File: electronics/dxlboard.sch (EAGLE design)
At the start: 49 parts

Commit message: Boards
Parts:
- R1, R12, R13, R14, R15, R18, R19, R2, R20, R21, R3, R4: value (none) -> 3K
- R7S1, R7S2, R8S, R8S1, R8S2, R8S3: value 20 -> 22
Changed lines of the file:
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@@
 <part name="C2" library="SparkFun-Passives" deviceset="CAP_POL" device="PTH2"/>
 <part name="GND15" library="supply1" deviceset="GND" device=""/>
-<part name="R1" library="rhoban" deviceset="RESISTANCE" device="-R0805"/>
-<part name="R2" library="rhoban" deviceset="RESISTANCE" device="-R0805"/>
-<part name="R3" library="rhoban" deviceset="RESISTANCE" device="-R0805"/>
+<part name="R1" library="rhoban" deviceset="RESISTANCE" device="-R0805" value="3K"/>
+<part name="R2" library="rhoban" deviceset="RESISTANCE" device="-R0805" value="3K"/>
+<part name="R3" library="rhoban" deviceset="RESISTANCE" device="-R0805" value="3K"/>
 <part name="GND23" library="supply1" deviceset="GND" device=""/>
 <part name="P+16" library="supply1" deviceset="VCC" device=""/>
 <part name="CA" library="rhoban" deviceset="C_EU" device="-100NF"/>
-<part name="R8S" library="rhoban" deviceset="RESISTANCE" device="-R0805" value="20"/>
+<part name="R8S" library="rhoban" deviceset="RESISTANCE" device="-R0805" value="22"/>
 <part name="USB" library="rhoban" deviceset="CONNEC_1X04" device=""/>
 <part name="GND16" library="supply1" deviceset="GND" device=""/>
@@
 <part name="R9" library="rhoban" deviceset="RESISTANCE" device="-R0805"/>
 <part name="GND18" library="supply1" deviceset="GND" device=""/>
-<part name="R4" library="rhoban" deviceset="RESISTANCE" device="-R0805"/>
+<part name="R4" library="rhoban" deviceset="RESISTANCE" device="-R0805" value="3K"/>
 <part name="P+1" library="supply1" deviceset="VCC" device=""/>
 <part name="GPIO1" library="rhoban" deviceset="CONNEC_1X09" device=""/>
@@
 <part name="GND5" library="supply1" deviceset="GND" device=""/>
 <part name="P+4" library="supply1" deviceset="VCC" device=""/>
-<part name="R12" library="rhoban" deviceset="RESISTANCE" device="-R0805"/>
-<part name="R13" library="rhoban" deviceset="RESISTANCE" device="-R0805"/>
-<part name="R14" library="rhoban" deviceset="RESISTANCE" device="-R0805"/>
+<part name="R12" library="rhoban" deviceset="RESISTANCE" device="-R0805" value="3K"/>
+<part name="R13" library="rhoban" deviceset="RESISTANCE" device="-R0805" value="3K"/>
+<part name="R14" library="rhoban" deviceset="RESISTANCE" device="-R0805" value="3K"/>
 <part name="GND6" library="supply1" deviceset="GND" device=""/>
 <part name="P+6" library="supply1" deviceset="VCC" device=""/>
 <part name="CA1" library="rhoban" deviceset="C_EU" device="-100NF"/>
-<part name="R7S1" library="rhoban" deviceset="RESISTANCE" device="-R0805" value="20"/>
-<part name="R8S1" library="rhoban" deviceset="RESISTANCE" device="-R0805" value="20"/>
-<part name="R15" library="rhoban" deviceset="RESISTANCE" device="-R0805"/>
+<part name="R7S1" library="rhoban" deviceset="RESISTANCE" device="-R0805" value="22"/>
+<part name="R8S1" library="rhoban" deviceset="RESISTANCE" device="-R0805" value="22"/>
+<part name="R15" library="rhoban" deviceset="RESISTANCE" device="-R0805" value="3K"/>
 <part name="P+11" library="supply1" deviceset="VCC" device=""/>
 <part name="R16" library="rhoban" deviceset="RESISTANCE" device="-R0805" value="2K"/>
@@
 <part name="GND13" library="supply1" deviceset="GND" device=""/>
 <part name="P+14" library="supply1" deviceset="VCC" device=""/>
-<part name="R18" library="rhoban" deviceset="RESISTANCE" device="-R0805"/>
-<part name="R19" library="rhoban" deviceset="RESISTANCE" device="-R0805"/>
-<part name="R20" library="rhoban" deviceset="RESISTANCE" device="-R0805"/>
+<part name="R18" library="rhoban" deviceset="RESISTANCE" device="-R0805" value="3K"/>
+<part name="R19" library="rhoban" deviceset="RESISTANCE" device="-R0805" value="3K"/>
+<part name="R20" library="rhoban" deviceset="RESISTANCE" device="-R0805" value="3K"/>
 <part name="GND17" library="supply1" deviceset="GND" device=""/>
 <part name="P+15" library="supply1" deviceset="VCC" device=""/>
 <part name="CA2" library="rhoban" deviceset="C_EU" device="-100NF"/>
-<part name="R7S2" library="rhoban" deviceset="RESISTANCE" device="-R0805" value="20"/>
-<part name="R8S2" library="rhoban" deviceset="RESISTANCE" device="-R0805" value="20"/>
-<part name="R21" library="rhoban" deviceset="RESISTANCE" device="-R0805"/>
+<part name="R7S2" library="rhoban" deviceset="RESISTANCE" device="-R0805" value="22"/>
+<part name="R8S2" library="rhoban" deviceset="RESISTANCE" device="-R0805" value="22"/>
+<part name="R21" library="rhoban" deviceset="RESISTANCE" device="-R0805" value="3K"/>
 <part name="P+17" library="supply1" deviceset="VCC" device=""/>
 <part name="R22" library="rhoban" deviceset="RESISTANCE" device="-R0805" value="2K"/>
@@
 <part name="GND19" library="supply1" deviceset="GND" device=""/>
 <part name="TTL3" library="rhoban" deviceset="CONNEC_1X03" device="_TTL"/>
-<part name="R8S3" library="rhoban" deviceset="RESISTANCE" device="-R0805" value="20"/>
+<part name="R8S3" library="rhoban" deviceset="RESISTANCE" device="-R0805" value="22"/>
 <part name="GPIO2" library="rhoban" deviceset="CONNEC_1X06" device=""/>
 </parts>

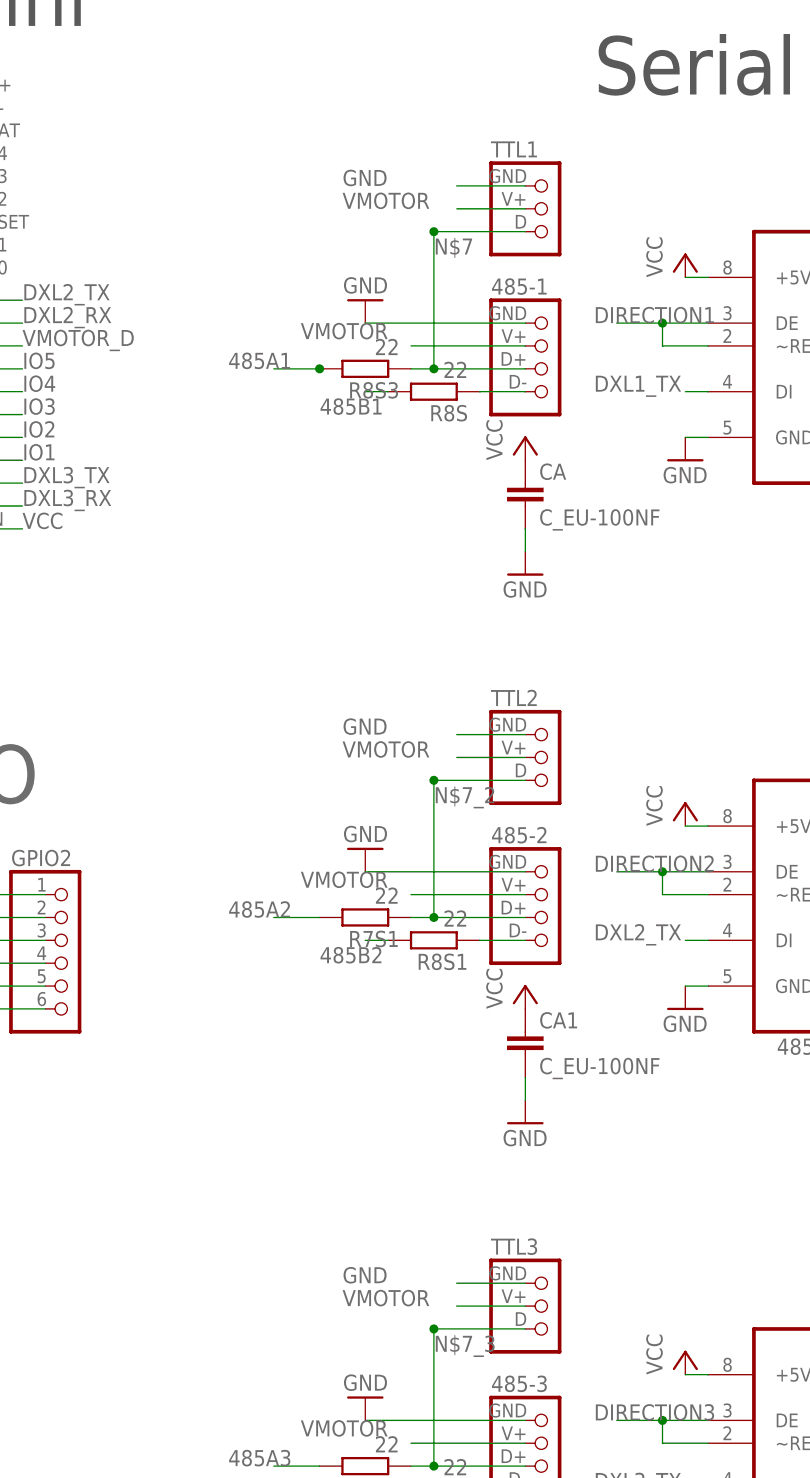
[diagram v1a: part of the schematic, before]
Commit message: Adding Farnell attributes
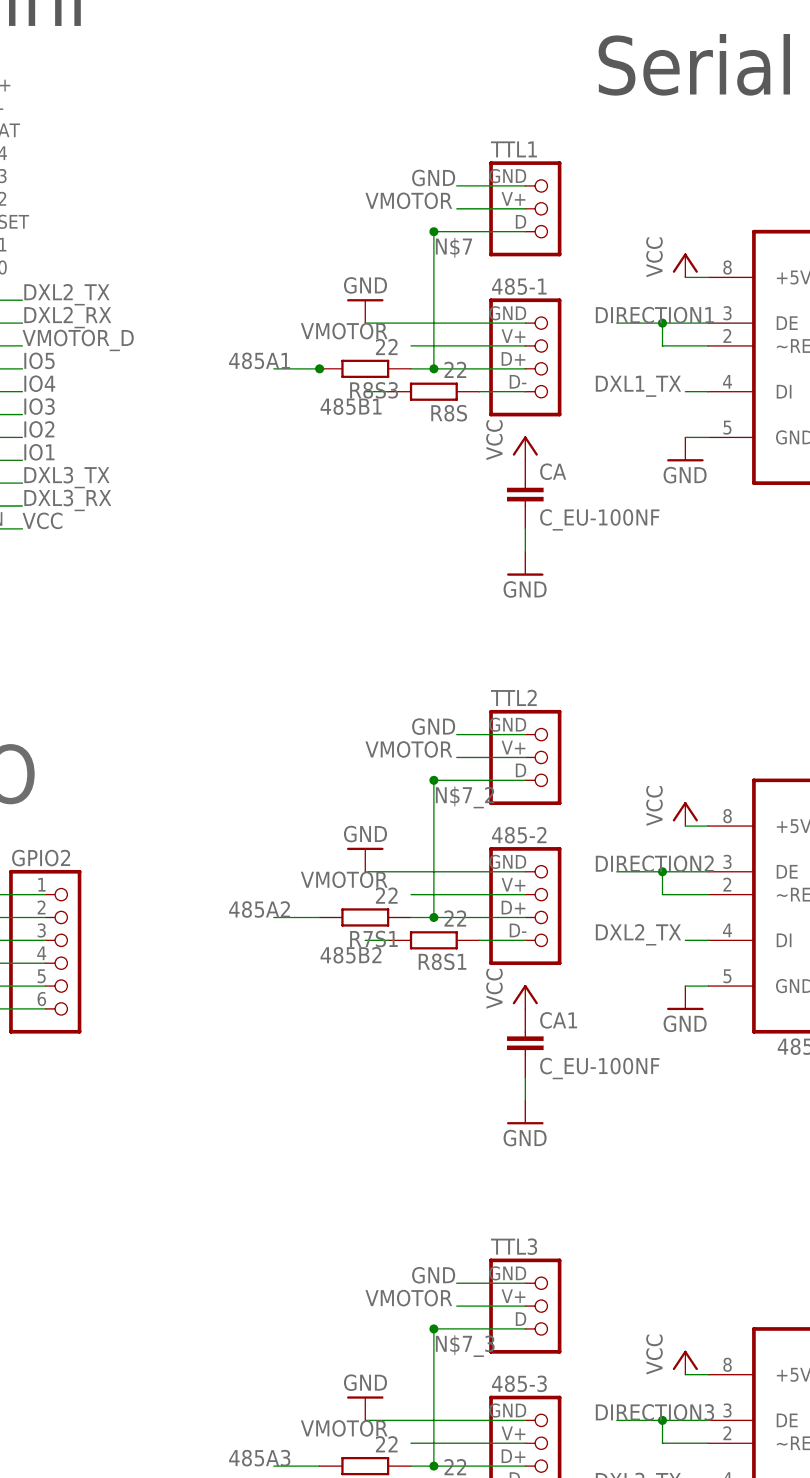
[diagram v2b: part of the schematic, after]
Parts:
- 485-1, 485-2, 485-3: FARNELL (none) -> 1104204
- D1: FARNELL (none) -> 8737843RL
- MAPLE: FARNELL (none) -> 1593469,1593469
- MAX1, MAX2, MAX485: FARNELL (none) -> 1564306
- TTL1, TTL2, TTL3: FARNELL (none) -> 9979620
- U$6: FARNELL (none) -> 1593463
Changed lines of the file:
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@@
 </classes>
 <parts>
-<part name="MAPLE" library="rhoban" deviceset="MAPLE_MINI" device=""/>
-<part name="485-1" library="rhoban" deviceset="CONNEC_1X04" device="_485"/>
+<part name="MAPLE" library="rhoban" deviceset="MAPLE_MINI" device="">
+<attribute name="FARNELL" value="1593469,1593469"/>
+</part>
+<part name="485-1" library="rhoban" deviceset="CONNEC_1X04" device="_485">
+<attribute name="FARNELL" value="1104204"/>
+</part>
 <part name="GND10" library="supply1" deviceset="GND" device=""/>
-<part name="MAX485" library="rhoban" deviceset="MAX485" device=""/>
+<part name="MAX485" library="rhoban" deviceset="MAX485" device="">
+<attribute name="FARNELL" value="1564306"/>
+</part>
 <part name="GND11" library="supply1" deviceset="GND" device=""/>
 <part name="P+7" library="supply1" deviceset="VCC" device=""/>
@@
 <part name="R5" library="rhoban" deviceset="RESISTANCE" device="-R0805" value="22"/>
 <part name="R6" library="rhoban" deviceset="RESISTANCE" device="-R0805" value="22"/>
-<part name="D1" library="SparkFun-DiscreteSemi" deviceset="DIODE" device="SOD"/>
+<part name="D1" library="SparkFun-DiscreteSemi" deviceset="DIODE" device="SOD">
+<attribute name="FARNELL" value="8737843RL"/>
+</part>
 <part name="R7" library="rhoban" deviceset="RESISTANCE" device="-R0805" value="1.5K"/>
 <part name="R8" library="rhoban" deviceset="RESISTANCE" device="-R0805"/>
@@
 <part name="R11" library="rhoban" deviceset="RESISTANCE" device="-R0805" value="3K"/>
 <part name="GND2" library="supply1" deviceset="GND" device=""/>
-<part name="U$6" library="rhoban" deviceset="GY-85" device=""/>
-<part name="TTL1" library="rhoban" deviceset="CONNEC_1X03" device="_TTL"/>
-<part name="485-2" library="rhoban" deviceset="CONNEC_1X04" device="_485"/>
+<part name="U$6" library="rhoban" deviceset="GY-85" device="">
+<attribute name="FARNELL" value="1593463"/>
+</part>
+<part name="TTL1" library="rhoban" deviceset="CONNEC_1X03" device="_TTL">
+<attribute name="FARNELL" value="9979620"/>
+</part>
+<part name="485-2" library="rhoban" deviceset="CONNEC_1X04" device="_485">
+<attribute name="FARNELL" value="1104204"/>
+</part>
 <part name="GND3" library="supply1" deviceset="GND" device=""/>
-<part name="MAX1" library="rhoban" deviceset="MAX485" device=""/>
+<part name="MAX1" library="rhoban" deviceset="MAX485" device="">
+<attribute name="FARNELL" value="1564306"/>
+</part>
 <part name="GND4" library="supply1" deviceset="GND" device=""/>
 <part name="P+2" library="supply1" deviceset="VCC" device=""/>
@@
 <part name="R17" library="rhoban" deviceset="RESISTANCE" device="-R0805" value="3K"/>
 <part name="GND7" library="supply1" deviceset="GND" device=""/>
-<part name="TTL2" library="rhoban" deviceset="CONNEC_1X03" device="_TTL"/>
-<part name="485-3" library="rhoban" deviceset="CONNEC_1X04" device="_485"/>
+<part name="TTL2" library="rhoban" deviceset="CONNEC_1X03" device="_TTL">
+<attribute name="FARNELL" value="9979620"/>
+</part>
+<part name="485-3" library="rhoban" deviceset="CONNEC_1X04" device="_485">
+<attribute name="FARNELL" value="1104204"/>
+</part>
 <part name="GND8" library="supply1" deviceset="GND" device=""/>
-<part name="MAX2" library="rhoban" deviceset="MAX485" device=""/>
+<part name="MAX2" library="rhoban" deviceset="MAX485" device="">
+<attribute name="FARNELL" value="1564306"/>
+</part>
 <part name="GND9" library="supply1" deviceset="GND" device=""/>
 <part name="P+12" library="supply1" deviceset="VCC" device=""/>
@@
 <part name="R23" library="rhoban" deviceset="RESISTANCE" device="-R0805" value="3K"/>
 <part name="GND19" library="supply1" deviceset="GND" device=""/>
-<part name="TTL3" library="rhoban" deviceset="CONNEC_1X03" device="_TTL"/>
+<part name="TTL3" library="rhoban" deviceset="CONNEC_1X03" device="_TTL">
+<attribute name="FARNELL" value="9979620"/>
+</part>
 <part name="R8S3" library="rhoban" deviceset="RESISTANCE" device="-R0805" value="22"/>
 <part name="GPIO2" library="rhoban" deviceset="CONNEC_1X06" device=""/>
@@
 </plain>
 <instances>
-<instance part="MAPLE" gate="G$1" x="-45.72" y="73.66"/>
-<instance part="485-1" gate="G$1" x="27.94" y="40.64"/>
+<instance part="MAPLE" gate="G$1" x="-45.72" y="73.66">
+<attribute name="FARNELL" x="-45.72" y="73.66" size="1.778" layer="96" display="off"/>
+</instance>
+<instance part="485-1" gate="G$1" x="27.94" y="40.64">
+<attribute name="FARNELL" x="27.94" y="40.64" size="1.778" layer="96" display="off"/>
+</instance>
 <instance part="GND10" gate="1" x="12.7" y="50.8" rot="R180"/>
-<instance part="MAX485" gate="A" x="68.58" y="48.26"/>
+<instance part="MAX485" gate="A" x="68.58" y="48.26">
+<attribute name="FARNELL" x="68.58" y="48.26" size="1.778" layer="96" display="off"/>
+</instance>
 <instance part="GND11" gate="1" x="48.26" y="33.02"/>
 <instance part="P+7" gate="VCC" x="48.26" y="55.88"/>
@@
 <instance part="R5" gate="G$1" x="-104.14" y="43.18"/>
 <instance part="R6" gate="G$1" x="-104.14" y="40.64"/>
-<instance part="D1" gate="G$1" x="-106.68" y="53.34" rot="R90"/>
+<instance part="D1" gate="G$1" x="-106.68" y="53.34" rot="R90">
+<attribute name="FARNELL" x="-106.68" y="53.34" size="1.778" layer="96" rot="R90" display="off"/>
+</instance>
 <instance part="R7" gate="G$1" x="-111.76" y="33.02" rot="R90"/>
 <instance part="R8" gate="G$1" x="-106.68" y="-22.86" rot="R90"/>
@@
 <instance part="R11" gate="G$1" x="106.68" y="68.58" rot="R180"/>
 <instance part="GND2" gate="1" x="114.3" y="68.58" rot="R90"/>
-<instance part="U$6" gate="G$1" x="-58.42" y="-73.66"/>
-<instance part="TTL1" gate="G$1" x="27.94" y="58.42"/>
-<instance part="485-2" gate="G$1" x="27.94" y="-20.32"/>
+<instance part="U$6" gate="G$1" x="-58.42" y="-73.66">
+<attribute name="FARNELL" x="-58.42" y="-73.66" size="1.778" layer="96" display="off"/>
+</instance>
+<instance part="TTL1" gate="G$1" x="27.94" y="58.42">
+<attribute name="FARNELL" x="27.94" y="58.42" size="1.778" layer="96" display="off"/>
+</instance>
+<instance part="485-2" gate="G$1" x="27.94" y="-20.32">
+<attribute name="FARNELL" x="27.94" y="-20.32" size="1.778" layer="96" display="off"/>
+</instance>
 <instance part="GND3" gate="1" x="12.7" y="-10.16" rot="R180"/>
-<instance part="MAX1" gate="A" x="68.58" y="-12.7"/>
+<instance part="MAX1" gate="A" x="68.58" y="-12.7">
+<attribute name="FARNELL" x="68.58" y="-12.7" size="1.778" layer="96" display="off"/>
+</instance>
 <instance part="GND4" gate="1" x="48.26" y="-27.94"/>
 <instance part="P+2" gate="VCC" x="48.26" y="-5.08"/>
@@
 <instance part="R17" gate="G$1" x="106.68" y="7.62" rot="R180"/>
 <instance part="GND7" gate="1" x="114.3" y="7.62" rot="R90"/>
-<instance part="TTL2" gate="G$1" x="27.94" y="-2.54"/>
-<instance part="485-3" gate="G$1" x="27.94" y="-81.28"/>
+<instance part="TTL2" gate="G$1" x="27.94" y="-2.54">
+<attribute name="FARNELL" x="27.94" y="-2.54" size="1.778" layer="96" display="off"/>
+</instance>
+<instance part="485-3" gate="G$1" x="27.94" y="-81.28">
+<attribute name="FARNELL" x="27.94" y="-81.28" size="1.778" layer="96" display="off"/>
+</instance>
 <instance part="GND8" gate="1" x="12.7" y="-71.12" rot="R180"/>
-<instance part="MAX2" gate="A" x="68.58" y="-73.66"/>
+<instance part="MAX2" gate="A" x="68.58" y="-73.66">
+<attribute name="FARNELL" x="68.58" y="-73.66" size="1.778" layer="96" display="off"/>
+</instance>
 <instance part="GND9" gate="1" x="48.26" y="-88.9"/>
 <instance part="P+12" gate="VCC" x="48.26" y="-66.04"/>
@@
 <instance part="R23" gate="G$1" x="106.68" y="-53.34" rot="R180"/>
 <instance part="GND19" gate="1" x="114.3" y="-53.34" rot="R90"/>
-<instance part="TTL3" gate="G$1" x="27.94" y="-63.5"/>
+<instance part="TTL3" gate="G$1" x="27.94" y="-63.5">
+<attribute name="FARNELL" x="27.94" y="-63.5" size="1.778" layer="96" display="off"/>
+</instance>
 <instance part="R8S3" gate="G$1" x="12.7" y="43.18" rot="R180"/>
 <instance part="GPIO2" gate="G$1" x="-25.4" y="-27.94"/>
@@
 <pinref part="TTL1" gate="G$1" pin="1"/>
 <wire x1="30.48" y1="63.5" x2="22.86" y2="63.5" width="0.1524" layer="91"/>
-<label x="10.16" y="63.5" size="1.778" layer="95"/>
+<label x="17.78" y="63.5" size="1.778" layer="95"/>
 </segment>
 <segment>
@@
 <pinref part="TTL2" gate="G$1" pin="1"/>
 <wire x1="30.48" y1="2.54" x2="22.86" y2="2.54" width="0.1524" layer="91"/>
-<label x="10.16" y="2.54" size="1.778" layer="95"/>
+<label x="17.78" y="2.54" size="1.778" layer="95"/>
 </segment>
 <segment>
@@
 <pinref part="TTL3" gate="G$1" pin="1"/>
 <wire x1="30.48" y1="-58.42" x2="22.86" y2="-58.42" width="0.1524" layer="91"/>
-<label x="10.16" y="-58.42" size="1.778" layer="95"/>
+<label x="17.78" y="-58.42" size="1.778" layer="95"/>
 </segment>
 <segment>
@@
 <pinref part="TTL1" gate="G$1" pin="2"/>
 <wire x1="30.48" y1="60.96" x2="22.86" y2="60.96" width="0.1524" layer="91"/>
-<label x="10.16" y="60.96" size="1.778" layer="95"/>
+<label x="12.7" y="60.96" size="1.778" layer="95"/>
 </segment>
 <segment>
@@
 <pinref part="TTL2" gate="G$1" pin="2"/>
 <wire x1="30.48" y1="0" x2="22.86" y2="0" width="0.1524" layer="91"/>
-<label x="10.16" y="0" size="1.778" layer="95"/>
+<label x="12.7" y="0" size="1.778" layer="95"/>
 </segment>
 <segment>
@@
 <pinref part="TTL3" gate="G$1" pin="2"/>
 <wire x1="30.48" y1="-60.96" x2="22.86" y2="-60.96" width="0.1524" layer="91"/>
-<label x="10.16" y="-60.96" size="1.778" layer="95"/>
+<label x="12.7" y="-60.96" size="1.778" layer="95"/>
 </segment>
 </net>
